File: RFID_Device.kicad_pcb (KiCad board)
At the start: 2 copper layers, 58 parts, among them IC1 NJU7223DL1-33-TE1, J1 USB_C_Receptacle_USB2.0_14P, J2 SM02B-SRSS-TB_LF__SN_, J3 541043431, U1 ESP32-S3-MINI-1-N8, U2 TPS2113APW, U3 MCP73831-2ACI_MC, U4 TPS61093DSKR, U5 MFRC52202HN1_157, U6 1SS383TE85L_F, Y1 27.12MHz

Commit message: Create PCB
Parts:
- removed IC1: NJU7223DL1-33-TE1, Footprints:TO-252-3-L1
- added C22: 1uF, Capacitor_SMD:C_0603_1608Metric, F.Cu at (135.0, 31.5)
- added C23: 1uF, Capacitor_SMD:C_0603_1608Metric, F.Cu at (127.0, 47.0)
- added C27: 1uF, Capacitor_SMD:C_0603_1608Metric, F.Cu at (138.6, 68.6)
- added C32: 4.7uF, Capacitor_SMD:C_0805_2012Metric, F.Cu at (122.5, 67.2)
- added L1: 10uH, Inductor_SMD:L_0805_2012Metric, F.Cu at (126.8, 75.0)
- added L2: 1mH, Inductor_SMD:L_1210_3225Metric, F.Cu at (127.0, 39.2)
- added L3: 1mH, Inductor_SMD:L_1210_3225Metric, F.Cu at (123.6, 39.2)
- added R18: 100K, Resistor_SMD:R_0402_1005Metric, F.Cu at (142.2, 56.5)
- added R19: 1.2M, Resistor_SMD:R_0402_1005Metric, F.Cu at (129.8, 53.1)
- added U7: 1SS383TE85L_F, Footprints:USQ_TOS, F.Cu at (141.6, 52.4)
- Antenna1, Antenna2: footprint TestPoint:TestPoint_Pad_D4.0mm -> TestPoint:TestPoint_Pad_D2.0mm
- C1: value 1F -> 1uF
- C10: value 0.1uF -> 4.7uF; footprint Capacitor_SMD:C_0603_1608Metric -> Capacitor_SMD:C_0805_2012Metric
- C11: value 10uF -> 1uF
- C13: value 1uF -> 0.1uF
- C3, C31, C6: footprint Capacitor_SMD:C_0603_1608Metric -> Capacitor_SMD:C_0805_2012Metric
- C30: value 4.7uF -> 1uF
- C8: value 4.7uF -> 10uF; footprint Capacitor_SMD:C_0603_1608Metric -> Capacitor_SMD:C_0805_2012Metric
- J1: value USB_C_Receptacle_USB2.0_14P -> 2171790001; footprint Connector_USB:USB_C_Receptacle_G-Switch_GT-USB-7010ASV -> Footprints:MOLEX_2171790001
- R1, R5: footprint Resistor_SMD:R_0603_1608Metric -> Resistor_SMD:R_0402_1005Metric
- R10: value 1K -> 10K; footprint Resistor_SMD:R_0603_1608Metric -> Resistor_SMD:R_0402_1005Metric
- R11, R12, R13, R14, R15: footprint Resistor_SMD:R_0603_1608Metric -> Resistor_SMD:R_1206_3216Metric
- R16: value 49.9 -> 1K; footprint Resistor_SMD:R_0603_1608Metric -> Resistor_SMD:R_1206_3216Metric
- R17: value 1.2M -> 100K; footprint Resistor_SMD:R_0603_1608Metric -> Resistor_SMD:R_0402_1005Metric
- R2: value 10k -> 5.1K; footprint Resistor_SMD:R_0603_1608Metric -> Resistor_SMD:R_0402_1005Metric
- R3: value 1k -> 10K; footprint Resistor_SMD:R_0603_1608Metric -> Resistor_SMD:R_0402_1005Metric
- R4: value 5.1K -> 1K; footprint Resistor_SMD:R_0603_1608Metric -> Resistor_SMD:R_1206_3216Metric
- R6: value 200K -> 2.7K; footprint Resistor_SMD:R_0603_1608Metric -> Resistor_SMD:R_1206_3216Metric
- R7: value 2k -> 100K; footprint Resistor_SMD:R_0603_1608Metric -> Resistor_SMD:R_0402_1005Metric
- R8: value 294K -> 100K; footprint Resistor_SMD:R_0603_1608Metric -> Resistor_SMD:R_0402_1005Metric
- R9: value 10.2K -> 330K; footprint Resistor_SMD:R_0603_1608Metric -> Resistor_SMD:R_1206_3216Metric
- U4: value TPS61093DSKR -> TLV1117LV33DCYR; footprint Footprints:SON50P250X250X80-11N -> Footprints:VREG_TLV1117LV33DCYR
- U5: value MFRC52202HN1_157 -> TPS61093DSKR; footprint Footprints:IC_PCAL9722HNMP -> Footprints:SON50P250X250X80-11N
- U6: value 1SS383TE85L_F -> MFRC52202HN1_115; footprint Footprints:USQ_TOS -> Package_DFN_QFN:HVQFN-32-1EP_5x5mm_P0.5mm_EP3.1x3.1mm
- Y1: value 27.12MHz -> ABM11AIG-27.120MHZ-4Z-T3; footprint Crystal:Crystal_HC18-U_Vertical -> Footprints:XTAL_ABM11AIG-27.120MHZ-4Z-T3
- moved C5 120.6 mm to (152.6, 81.6), turned to 90 degrees
- moved C4 120.4 mm to (152.6, 78.4), turned to 90 degrees
- moved C6 119.7 mm to (156.8, 68.8), turned to 180 degrees
- moved C7 119.6 mm to (156.8, 70.8), turned to 180 degrees
- moved R2 116.6 mm to (155.6, 78.1), turned to 180 degrees
- moved C8 116.6 mm to (156.4, 60.4)
- moved J2 115.9 mm to (157.8, 56.3), turned to 180 degrees
- moved R5 113.7 mm to (155.6, 75.1)
- moved J1 111.6 mm to (161.3, 76.8), turned to 90 degrees
- moved R4 109.7 mm to (152.4, 68.8), turned to 180 degrees
- moved U3 107.2 mm to (154.4, 64.6), turned to 180 degrees
- moved R6 106.6 mm to (150.8, 65.0), turned to 90 degrees
- moved C9 105.6 mm to (141.4, 78.6), turned to 180 degrees
- moved R3 104.6 mm to (142.5, 81.2), turned to 180 degrees
- moved C10 101.6 mm to (137.0, 81.8), turned to 90 degrees
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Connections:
- net IO 19 renamed USB_N
- net IO 20 renamed USB_P
- C10 pad 1: Net-(U4-CP2) -> GND
- C10 pad 2: Net-(U4-CP1) -> 3V3
- C11 pad 2: BAT_P -> Net-(U5-SS)
- C12 pad 1: Net-(U4-VO) -> Net-(U5-CP2)
- C12 pad 2: GND -> Net-(U5-CP1)
- C13 pad 1: GND -> Net-(U5-VO)
- C13 pad 2: /Power/15V -> GND
- C14 pad 2: Net-(U5-OSCIN) -> 17V
- C15 pad 1: GND -> Net-(U6-OSCIN)
- C15 pad 2: Net-(U5-OSCOUT) -> GND
- C17 pad 1: Net-(C17-Pad1) -> TX3
- C18 pad 1: TX3 -> Net-(C17-Pad2)
- C18 pad 2: Net-(C17-Pad1) -> Net-(C18-Pad2)
- C20 pad 1: Net-(C20-Pad1) -> TX3
- C20 pad 2: GND -> Net-(C20-Pad2)
- C21 pad 1: GND -> Net-(C18-Pad2)
- C24 pad 1: Net-(U5-VMID) -> GND
- C24 pad 2: GND -> Net-(C21-Pad2)
- C25 pad 1: Net-(U5-RX) -> Net-(U6-VMID)
- C25 pad 2: Net-(C25-Pad2) -> GND
- C26 pad 1: GND -> Net-(U6-RX)
- C26 pad 2: 3V3 -> Net-(C26-Pad2)
- C28 pad 1: Net-(C28-Pad1) -> 3V3
- C29 pad 1: GND -> Net-(C29-Pad1)
- C29 pad 2: Net-(C29-Pad2) -> GND
- C30 pad 1: 17V -> GND
- C30 pad 2: GND -> Net-(C30-Pad2)
- C31 pad 1: Net-(C31-Pad1) -> 17V
- C8 pad 2: 3V3 -> BAT_P
- C9 pad 1: GND -> Net-(U4-OUT_2)
- C9 pad 2: Net-(U4-SS) -> 3V3
- J1 pad A8: (no net) -> unconnected-(J1-SBU1-PadA8)
- J1 pad B8: (no net) -> unconnected-(J1-SBU2-PadB8)
- J3 pad 10: Net-(C29-Pad2) -> Net-(C30-Pad2)
- J3 pad 3: Net-(C31-Pad1) -> Net-(C32-Pad1)
- J3 pad 32: Net-(C31-Pad1) -> Net-(C32-Pad1)
- J3 pad 6: Net-(C28-Pad1) -> Net-(C29-Pad1)
- J3 pad 9: Net-(C29-Pad2) -> Net-(C30-Pad2)
- R10 pad 1: IO 10 -> GND
- R10 pad 2: 3V3 -> Net-(U5-FB)
- R11 pad 1: Net-(Antenna1-Pad1) -> IO 10
- R11 pad 2: Net-(C20-Pad1) -> 3V3
- R12 pad 1: Net-(Antenna2-Pad1) -> Net-(Antenna1-Pad1)
- R12 pad 2: Net-(C21-Pad2) -> Net-(C20-Pad2)
- R13 pad 1: Net-(U5-RX) -> Net-(Antenna2-Pad1)
- R13 pad 2: Net-(U5-VMID) -> Net-(C21-Pad2)
- R14 pad 1: IO 12 -> Net-(U6-RX)
- R14 pad 2: 3V3 -> Net-(U6-VMID)
- R15 pad 1: TX3 -> IO 12
- R15 pad 2: Net-(C25-Pad2) -> 3V3
- R16 pad 1: Net-(J3-Pad7) -> TX3
- R16 pad 2: Net-(R16-Pad2) -> Net-(C26-Pad2)
- R17 pad 1: GND -> Net-(J3-Pad7)
- R17 pad 2: Net-(J3-Pad29) -> Net-(R17-Pad2)
- R2 pad 1: Net-(U2-ILIM) -> Net-(J1-CC1)
- R3 pad 1: USB_5V -> Net-(U2-ILIM)
- R3 pad 2: Net-(U3-STAT) -> GND
- R4 pad 1: GND -> USB_5V
- R4 pad 2: Net-(J1-CC1) -> Net-(U3-STAT)
- R5 pad 1: Net-(J1-CC2) -> GND
- R5 pad 2: GND -> Net-(J1-CC2)
- R6 pad 1: GND -> Net-(U3-PROG)
- R6 pad 2: Net-(U4-SS) -> GND
- R7 pad 1: Net-(U3-PROG) -> Net-(R7-Pad1)
- R7 pad 2: GND -> Net-(U5-SS)
- R8 pad 1: Net-(U4-FB) -> GND
- R8 pad 2: /Power/15V -> Net-(R7-Pad1)
- R9 pad 1: GND -> Net-(U5-FB)
- R9 pad 2: Net-(U4-FB) -> 17V
- U2 pad 7: Net-(IC1-VIN) -> Net-(U2-OUT)
- U4 pad 2: 3V3 -> Net-(U4-OUT_2)
- U4 pad 3: Net-(U4-CP2) -> Net-(U2-OUT)
- U4 pad 4: Net-(U4-CP1) -> unconnected-(U4-OUT_4-Pad4)
- U5 pad 1: 3V3 -> GND
- U5 pad 10: GND -> Net-(U5-VO)
- U5 pad 11: TX1 -> unconnected-(U5-EPAD-Pad11)
- U5 pad 3: 3V3 -> Net-(U5-CP2)
- U5 pad 4: GND -> Net-(U5-CP1)
- U5 pad 5: GND -> IO 21
- U5 pad 6: IO 9 -> Net-(U5-SS)
- U5 pad 7: unconnected-(U5-MFIN-Pad7) -> Net-(U5-FB)
- U5 pad 8: unconnected-(U5-MFOUT-Pad8) -> 17V
- U5 pad 9: unconnected-(U5-SVDD-Pad9) -> Net-(U5-SW)
- U6 pad 1: Net-(U6-Pad1) -> 3V3
- U6 pad 2: Net-(R16-Pad2) -> 3V3
- U6 pad 3: Net-(U6-Pad1) -> 3V3
- Y1 pad 1: Net-(U5-OSCIN) -> Net-(U6-OSCIN)
- Y1 pad 2: Net-(U5-OSCOUT) -> GND
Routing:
- net 3V3: track 0.00 -> 190.4 mm, vias 0 -> 6
- net GND: track 0.00 -> 169.2 mm, vias 0 -> 85
- net IO 21: track 0.00 -> 59.7 mm, vias 0 -> 2
- net USB_N: track 0.00 -> 55.2 mm, vias 0 -> 2
- net USB_P: track 0.00 -> 53.7 mm, vias 0 -> 4
- net IO 36: track 0.00 -> 45.3 mm, vias 0 -> 2
- net IO 35: track 0.00 -> 42.6 mm, vias 0 -> 2
- net IO 5: track 0.00 -> 39.2 mm
- net IO 34: track 0.00 -> 38.2 mm, vias 0 -> 2
- net IO 6: track 0.00 -> 38.0 mm
- net BAT_P: track 0.00 -> 37.4 mm, vias 0 -> 2
- net USB_5V: track 0.00 -> 37.1 mm
- net IO 9: track 0.00 -> 35.7 mm, vias 0 -> 3
- net 17V: track 0.00 -> 30.6 mm, vias 0 -> 2
- net IO 12: track 0.00 -> 28.4 mm, vias 0 -> 4
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- added copper zone on In2.Cu, net GND
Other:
- board outline added: 45 x 71 mm
- copper layers 2 -> 4

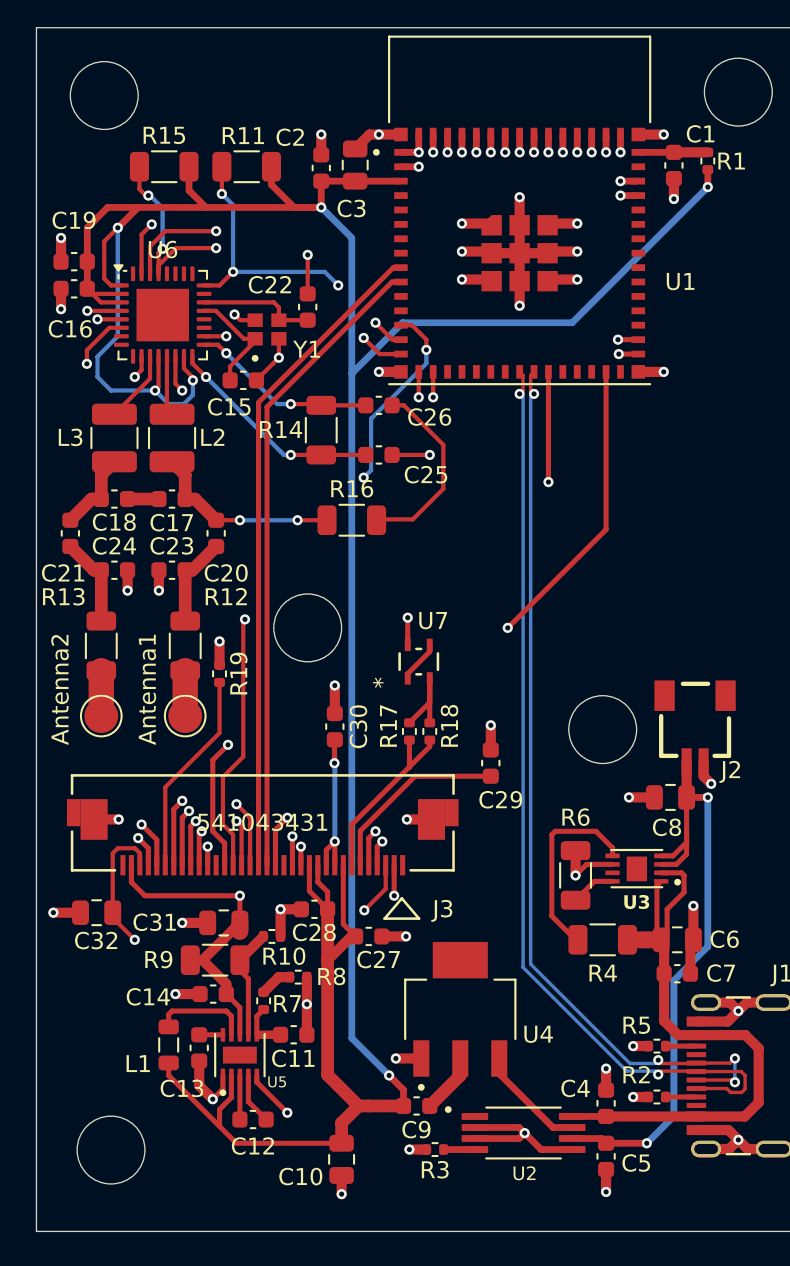
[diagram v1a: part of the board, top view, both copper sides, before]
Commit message: Fix minor design mistakes
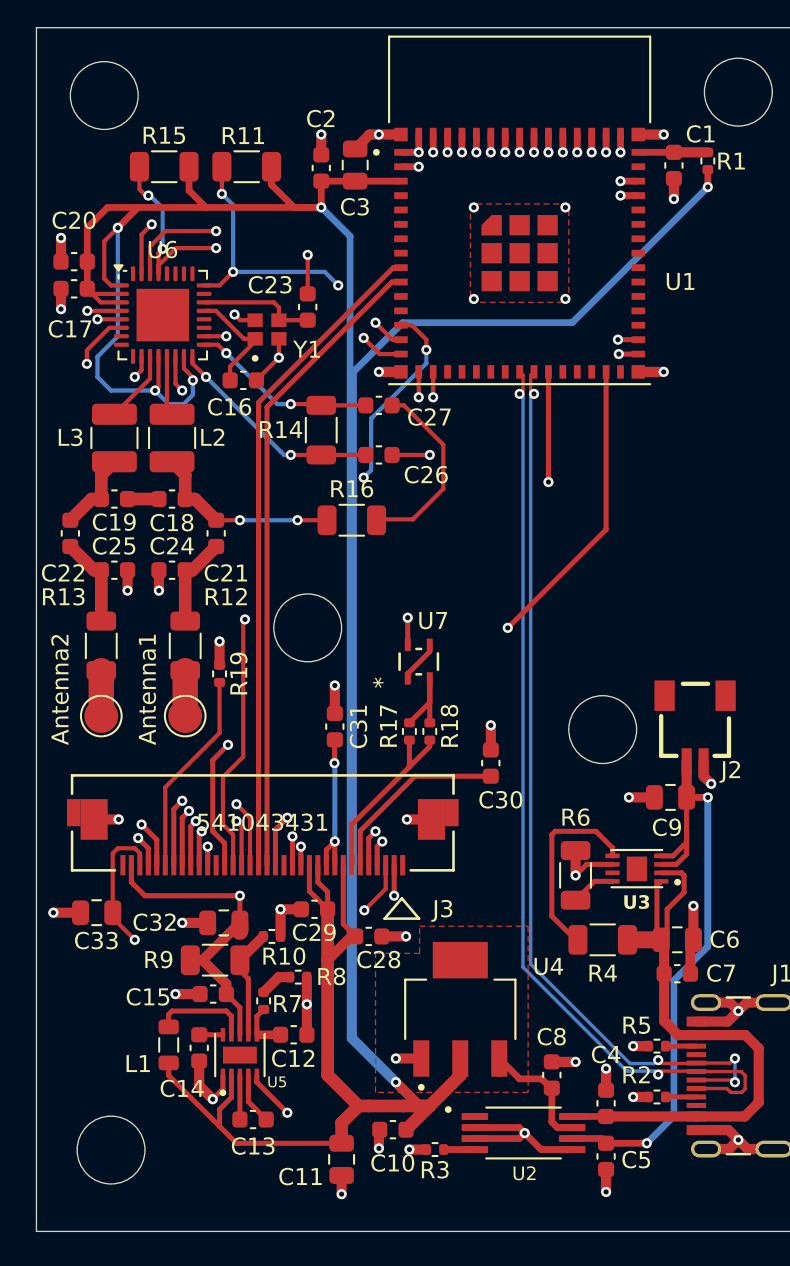
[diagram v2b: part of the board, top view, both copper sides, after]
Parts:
- added C8: 1uF, Capacitor_SMD:C_0603_1608Metric, F.Cu at (149.4, 76.8)
- added G***: LOGO, LOGO, B.Cu at (150.8, 24.6)
- added G***: LOGO, LOGO, B.Cu at (142.6, 51.0)
- moved C10 1.98 mm to (140.0, 80.0)
- renumbered C9 to C10, C10 to C11, C11 to C12, C12 to C13, C13 to C14, C14 to C15, C15 to C16, C16 to C17, C17 to C18, C18 to C19, C19 to C20, C20 to C21, C21 to C22, C22 to C23, C23 to C24, C24 to C25, C25 to C26, C26 to C27, C27 to C28, C28 to C29, C29 to C30, C30 to C31, C31 to C32, C32 to C33, C8 to C9
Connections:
- C10 pad 1: Net-(U4-OUT_2) -> 3V3
- C10 pad 2: 3V3 -> GND
- U4 pad 2: Net-(U4-OUT_2) -> 3V3
- U4 pad 4: unconnected-(U4-OUT_4-Pad4) -> 3V3
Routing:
- net GND: track 169.2 -> 152.0 mm, vias 85 -> 83
- net 3V3: track 190.4 -> 198.0 mm
- net Net-(U4-OUT_2): track 3.55 -> 0.00 mm
- net Net-(U2-OUT): track 6.51 -> 8.03 mm
- added copper zone on F.Cu, net 3V3
- added copper zone on F.Cu, net GND
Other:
- board text added: "{dblquote}A punch to the face, puts a bitch in her place{dblquote} Sun Tzu, The Art of War"

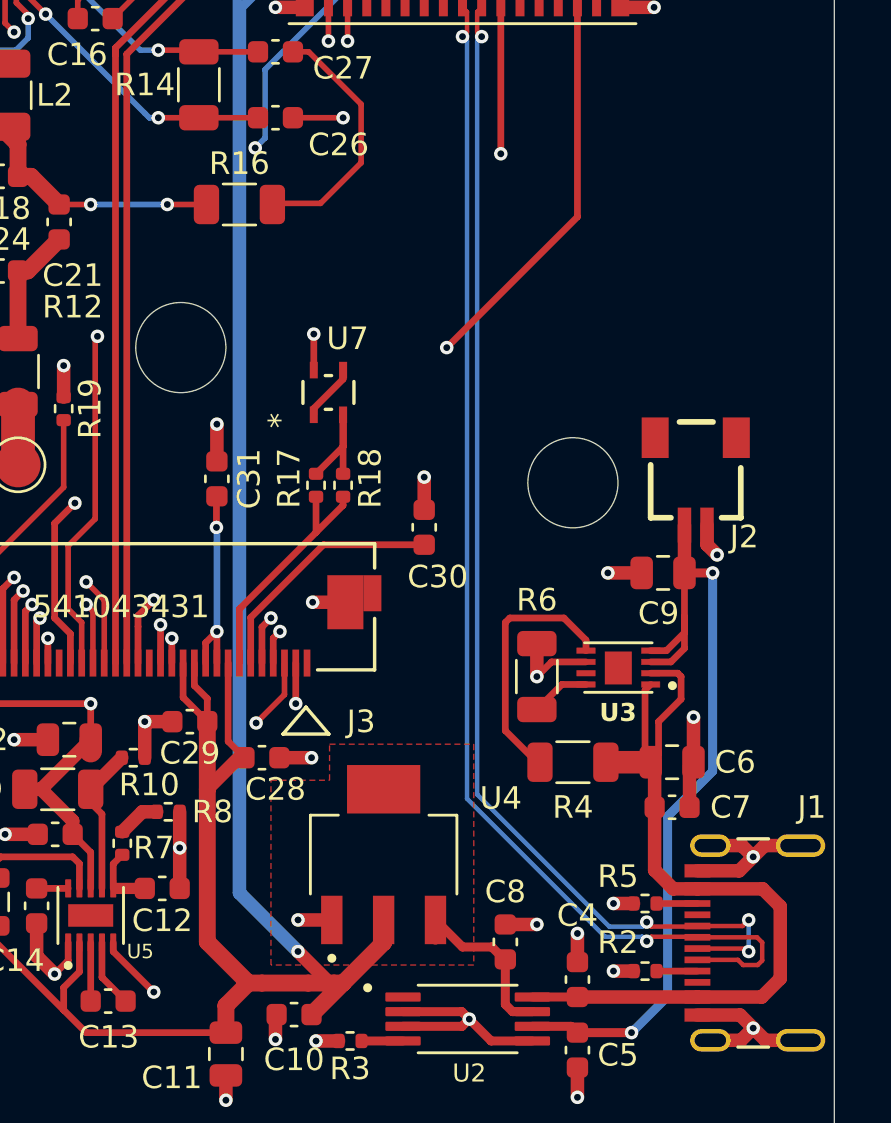
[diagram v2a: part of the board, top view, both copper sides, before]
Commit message: Fix minor design mistakes
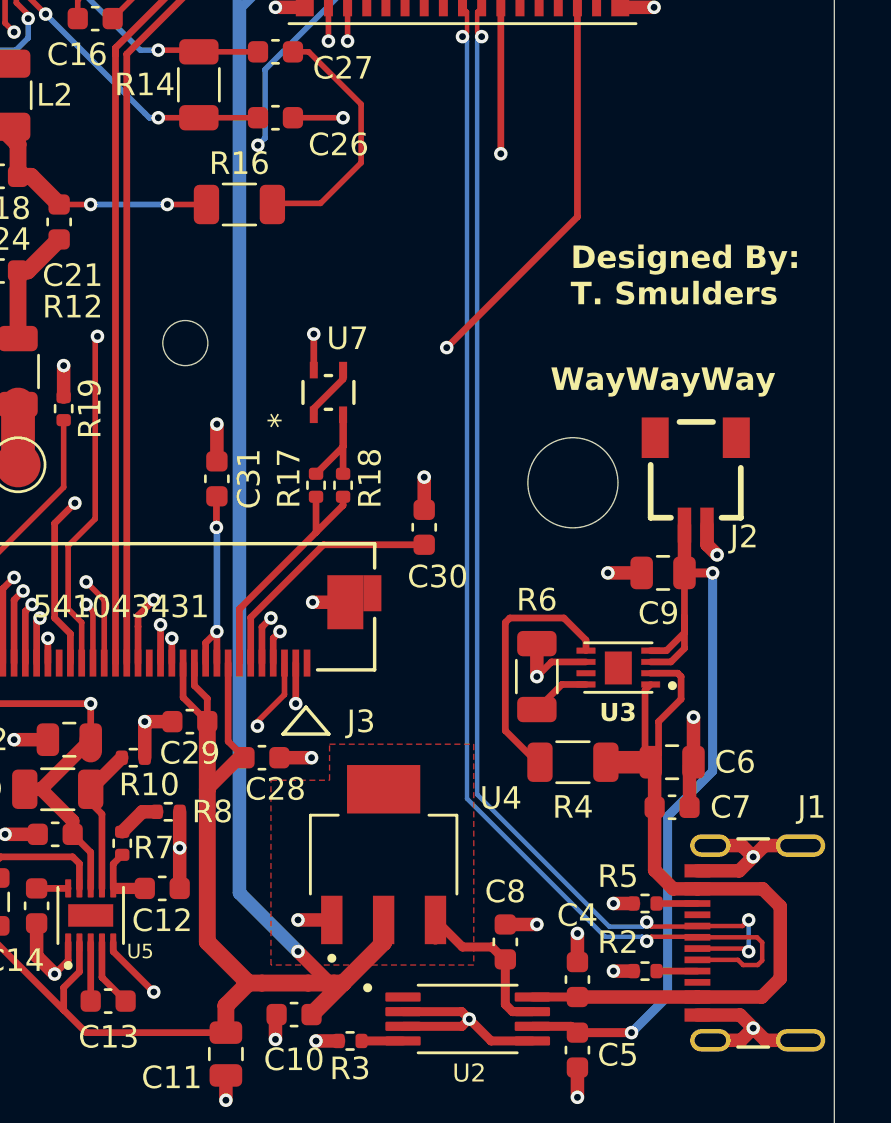
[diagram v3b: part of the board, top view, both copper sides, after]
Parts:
- removed the G*** at (150.8, 24.6)
- removed the G*** at (142.6, 51.0)
- added G***: LOGO, LOGO, B.Cu at (147.7, 44.9)
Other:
- outline, holes or cut-outs redrawn
- board text added: "Designed By: T. Smulders"
- board text added: "Repair Guide"
- board text added: "WayWayWay"
- board text removed: "{dblquote}A punch to the face, puts a bitch in her place{dblquote} Sun Tzu, The Art of War"
